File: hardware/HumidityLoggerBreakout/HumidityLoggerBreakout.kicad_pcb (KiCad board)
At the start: 2 copper layers, 75 x 52 mm, 43 parts, among them J1 Barrel_Jack_Switch, J10 RELAY_PWR, J2 POWER_IN, J3 LEVEL, J4 RELAY, J5 MCU_PWR, J6 Conn_01x11, J7 Conn_01x11, J8 I2C, J9 I2C_OUT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

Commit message: The big connectors were flipped :(
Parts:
- moved J6 48.0 mm to (141.2, 52.0)
- moved J7 48.0 mm to (141.2, 100.0)
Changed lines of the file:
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@@
   )
   (footprint "Connector_PinHeader_2.54mm:PinHeader_1x11_P2.54mm_Vertical" (layer "F.Cu")
-    (at 141.15 100 -90)
+    (at 141.15 52 -90)
     (descr "Through hole straight pin header, 1x11, 2.54mm pitch, single row")
     (tags "Through hole pin header THT 1x11 2.54mm single row")
@@
   )
   (footprint "Connector_PinHeader_2.54mm:PinHeader_1x11_P2.54mm_Vertical" (layer "F.Cu")
-    (at 141.15 52 -90)
+    (at 141.15 100 -90)
     (descr "Through hole straight pin header, 1x11, 2.54mm pitch, single row")
     (tags "Through hole pin header THT 1x11 2.54mm single row")

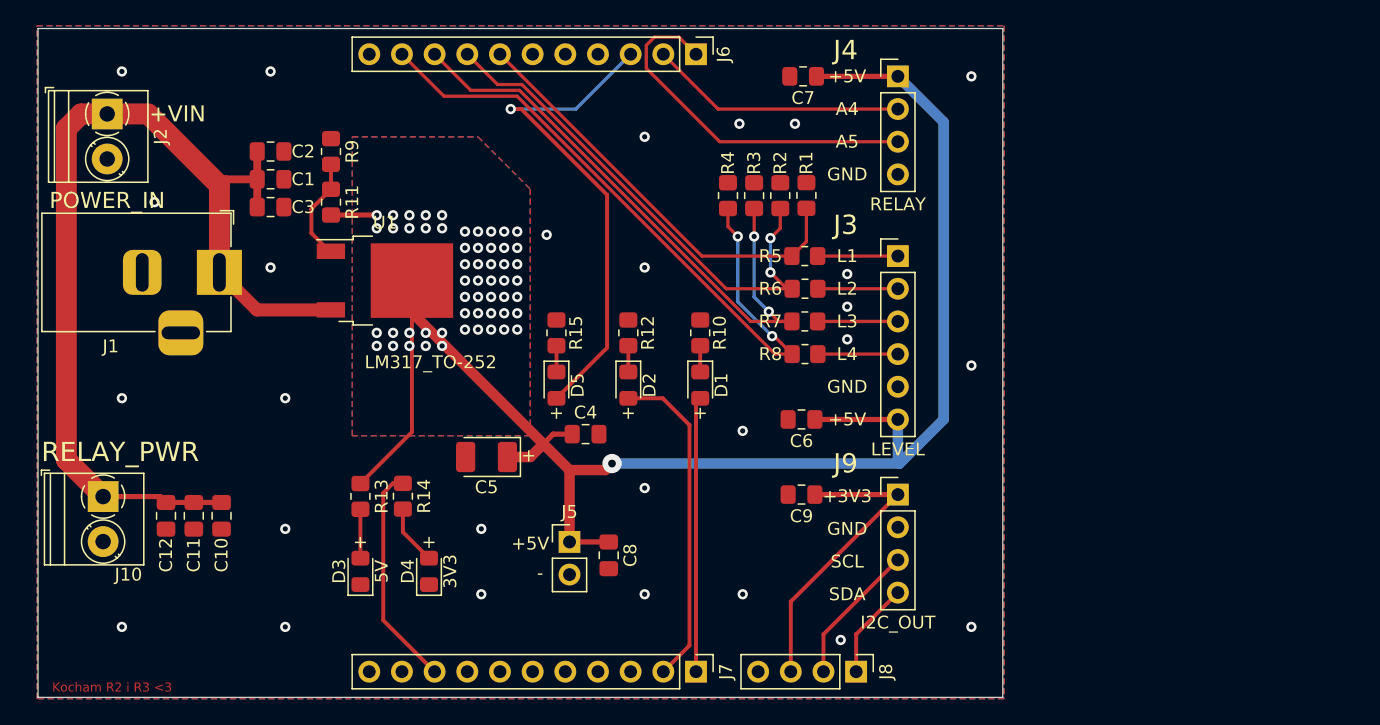
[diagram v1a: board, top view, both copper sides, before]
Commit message: Fixed the connectors to Maduino.
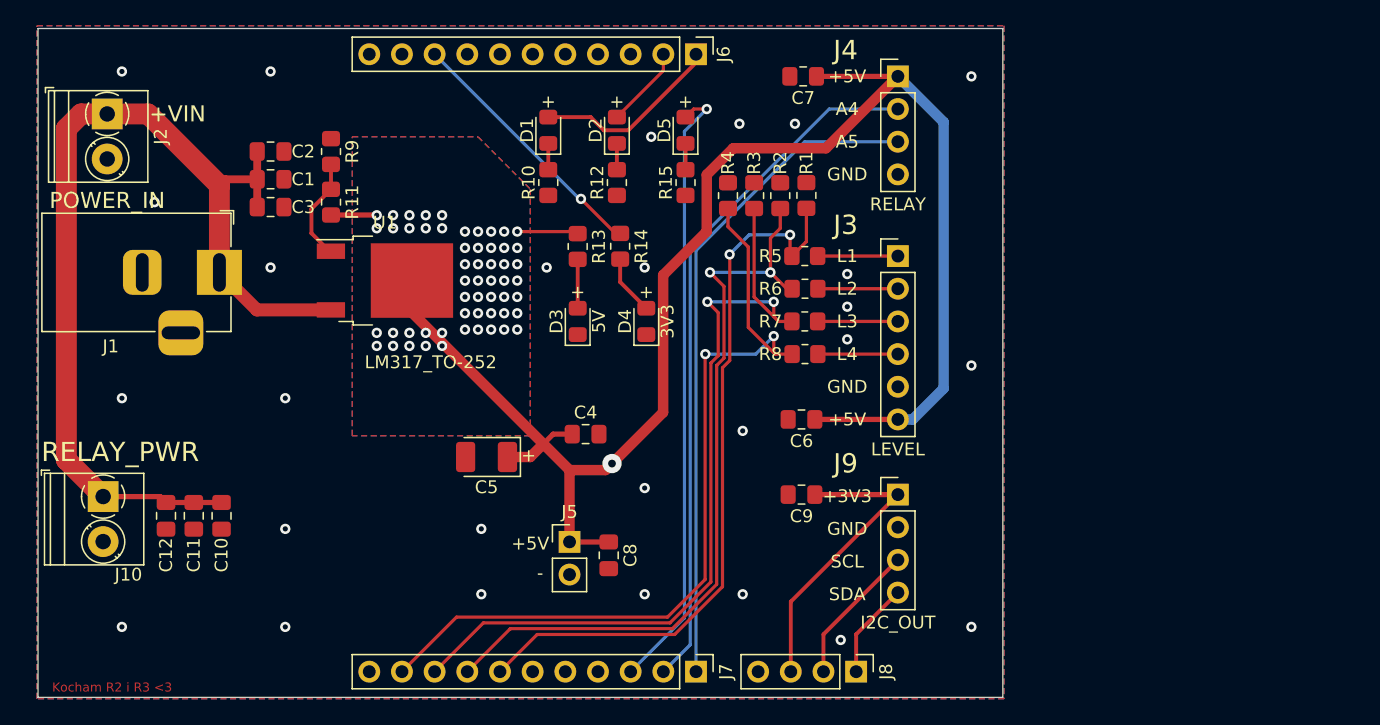
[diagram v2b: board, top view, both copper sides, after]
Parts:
- moved R13 25.7 mm to (132.0, 66.9)
- moved D3 25.7 mm to (132.0, 72.8)
- moved D4 25.7 mm to (137.3, 72.8)
- moved R14 25.7 mm to (135.3, 66.9)
- moved D1 23.1 mm to (129.7, 57.9), turned to 90 degrees
- moved D5 22.2 mm to (140.3, 57.9), turned to 90 degrees
- moved D2 19.8 mm to (135.0, 57.9), turned to 90 degrees
- moved R10 16.6 mm to (129.7, 62.0), turned to -90 degrees
- moved R15 15.4 mm to (140.3, 62.0), turned to -90 degrees
- moved R12 11.7 mm to (135.0, 62.0), turned to -90 degrees
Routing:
- net /A4: track 20.0 -> 54.4 mm
- net /D10: track 33.4 -> 57.3 mm, vias 0 -> 2
- net /A5: track 28.4 -> 51.9 mm
- net /D3: track 25.6 -> 6.38 mm
- net /D11: track 40.3 -> 59.3 mm
- net /D12: track 47.0 -> 64.2 mm
- net /D13: track 53.5 -> 65.6 mm
- net /A3: track 38.8 -> 48.1 mm
- net /D2: track 21.4 -> 15.5 mm
- net +3.3V: track 41.1 -> 43.9 mm, vias 0 -> 1
- net +5V: track 130.3 -> 132.7 mm
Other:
- board text added: "Hubert the Humidity Logger v1.1 Marcin Dymczyk 2023"
- board text removed: "Hubert the Humidity Logger Marcin Dymczyk 2023"

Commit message: Minor.
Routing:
- net +5V: vias 56 -> 55
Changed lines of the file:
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@@
   (via (at 126.238 73.406) (size 0.8) (drill 0.4) (layers "F.Cu" "B.Cu") (free) (net 3))
   (via (at 127.254 65.786) (size 0.8) (drill 0.4) (layers "F.Cu" "B.Cu") (free) (net 3))
-  (via (at 134.62 83.82) (size 1.5) (drill 0.6) (layers "F.Cu" "B.Cu") (net 3))
   (via (at 125.222 73.406) (size 0.8) (drill 0.4) (layers "F.Cu" "B.Cu") (free) (net 3))
   (via (at 123.19 67.056) (size 0.8) (drill 0.4) (layers "F.Cu" "B.Cu") (free) (net 3))
@@
   (segment (start 129.667 58.937) (end 129.667 60.976) (width 0.3048) (layer "F.Cu") (net 4))
   (segment (start 141.15 52.652) (end 141.15 52) (width 0.3048) (layer "F.Cu") (net 5))
-  (segment (start 129.667 56.887) (end 129.995 56.559) (width 0.3048) (layer "F.Cu") (net 5))
   (segment (start 135.89 57.912) (end 133.985 57.912) (width 0.3048) (layer "F.Cu") (net 5))
   (segment (start 129.413 56.887) (end 132.96 56.887) (width 0.3048) (layer "F.Cu") (net 5))
@@
   (segment (start 149.733 66.564) (end 148.606 67.691) (width 0.254) (layer "F.Cu") (net 23))
   (segment (start 125.91 100) (end 128.802 97.108) (width 0.25) (layer "F.Cu") (net 23))
-  (segment (start 143.209 93.396188) (end 143.211 93.394188) (width 0.254) (layer "F.Cu") (net 23))
   (segment (start 139.497188 97.108) (end 143.209 93.396188) (width 0.25) (layer "F.Cu") (net 23))
   (segment (start 143.209 93.396188) (end 143.209 76.376792) (width 0.25) (layer "F.Cu") (net 23))

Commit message: Modified the schematic to drop unnecessary features.
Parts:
- removed J5: MCU_PWR, Connector_PinHeader_2.54mm:PinHeader_1x02_P2.54mm_Vertical
- added D6: LOW, LED_SMD:LED_0805_2012Metric_Pad1.15x1.40mm_HandSolder, F.Cu at (181.7, 80.1)
- added D7: OK, LED_SMD:LED_0805_2012Metric_Pad1.15x1.40mm_HandSolder, F.Cu at (186.0, 73.5)
- added D8: HIGH, LED_SMD:LED_0805_2012Metric_Pad1.15x1.40mm_HandSolder, F.Cu at (176.9, 80.1)
- added D9: VHIGH, LED_SMD:LED_0805_2012Metric_Pad1.15x1.40mm_HandSolder, F.Cu at (186.0, 70.5)
- J10: value RELAY_PWR -> PWR_OUT
- J2: value POWER_IN -> PWR_IN
- J3: value LEVEL -> MCU_PWR; footprint Connector_PinHeader_2.54mm:PinHeader_1x06_P2.54mm_Vertical -> TerminalBlock_Phoenix:TerminalBlock_Phoenix_PT-1,5-2-3.5-H_1x02_P3.50mm_Horizontal
- J4: value RELAY -> IO
- J8: value I2C -> I2C_MCU
- R1, R2, R3, R4: value 2k -> 1k
- moved R4 48.2 mm to (190.7, 73.4), turned to 0 degrees
- moved R3 42.5 mm to (186.0, 76.5), turned to 0 degrees
- moved R2 42.1 mm to (186.5, 79.5), turned to 0 degrees
- moved R1 41.7 mm to (190.7, 70.4), turned to 0 degrees
- moved J3 21.2 mm to (177.3, 73.1)
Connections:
- J3 pad 1: Net-(J3-Pad1) -> GND
- J3 pad 2: Net-(J3-Pad2) -> +5V
- R1 pad 1: GND -> Net-(D6-Pad1)
- R1 pad 2: /D10 -> GND
- R2 pad 1: GND -> Net-(D7-Pad1)
- R2 pad 2: /D11 -> GND
- R3 pad 1: GND -> Net-(D8-Pad1)
- R3 pad 2: /D12 -> GND
- R4 pad 1: GND -> Net-(D9-Pad1)
- R4 pad 2: /D13 -> GND
- R5 pad 2: Net-(J3-Pad1) -> Net-(D9-Pad2)
- R6 pad 2: Net-(J3-Pad2) -> Net-(D8-Pad2)
- R7 pad 2: Net-(J3-Pad3) -> Net-(D7-Pad2)
- R8 pad 2: Net-(J3-Pad4) -> Net-(D6-Pad2)
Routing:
- net Net-(J3-Pad3): track 6.24 -> 0.00 mm
- net Net-(J3-Pad1): track 6.24 -> 0.00 mm
- net Net-(D9-Pad2): track 0.00 -> 6.24 mm
- net Net-(D7-Pad2): track 0.00 -> 6.24 mm
- net Net-(J3-Pad4): track 6.22 -> 0.00 mm
- net Net-(J3-Pad2): track 6.22 -> 0.00 mm
- net Net-(D8-Pad2): track 0.00 -> 6.22 mm
- net Net-(D6-Pad2): track 0.00 -> 6.22 mm
